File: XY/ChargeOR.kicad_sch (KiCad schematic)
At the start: 8 parts, among them U13 LTC4376CDHD_PBF, U9 SI3865DDV-T1-GE3

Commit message: MPPT fixes
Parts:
- removed C48: 10uF, Capacitor_SMD:C_1206_3216Metric, symbol Device:C_Small
- removed C49: 1nF, Capacitor_SMD:C_0603_1608Metric, symbol Device:C_Small
- removed C50: 1uF, Capacitor_SMD:C_1206_3216Metric, symbol Device:C_Small
- removed D7: LSM115, SolarPanels:DO-214BA_MCH, symbol Device:D_Schottky_Small
- removed R92: 100K, Resistor_SMD:R_0603_1608Metric, symbol Device:R_Small
- removed R93: 10K, Resistor_SMD:R_0603_1608Metric, symbol Device:R_Small
- removed U13: LTC4376CDHD_PBF, Package_DFN_QFN:DFN-16-1EP_4x5mm_P0.5mm_EP2.44x4.34mm, symbol SolarPanels:LTC4376CDHD_PBF
- removed U9: SI3865DDV-T1-GE3, Package_TO_SOT_SMD:SOT-23-6, symbol SolarPanels:SI3865DDV-T1-GE3
- added C42: 0.1uF, Capacitor_SMD:C_0603_1608Metric, symbol Device:C_Small
- added D8: PMEG4005EH, Diode_SMD:D_SOD-123F, symbol Diode:PMEG4005EH
- added U7: LTC4412xS6, Package_TO_SOT_SMD:TSOT-23-6, symbol Power_Management:LTC4412xS6
- added U8: SIRA99DP-T1-GE3, SolarPanels:MOSFET_7DP-T1-GE3_VIS, symbol Argus-Misc:SIRA99DP-T1-GE3
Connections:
- net GND: now also C42.2, U7.2 (GND), U7.3 (CTL)
- net IN: now also C42.1, D8.2 (A), U7.1 (VIN), U8.5 (D), U8.6 (D), U8.7 (D), U8.8 (D)
- net OUT: now also D8.1 (K), U7.6 (SENSE), U8.1 (S), U8.2 (S), U8.3 (S)
- new net: U7.5 (GATE), U8.4 (G)

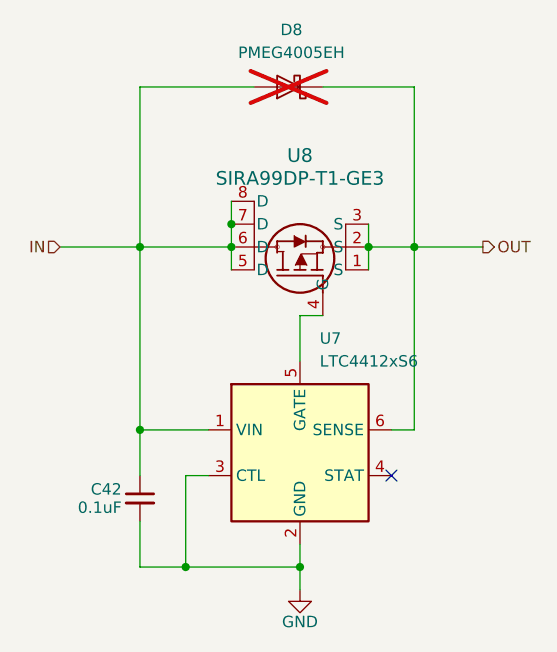
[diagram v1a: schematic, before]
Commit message: Added address breakouts
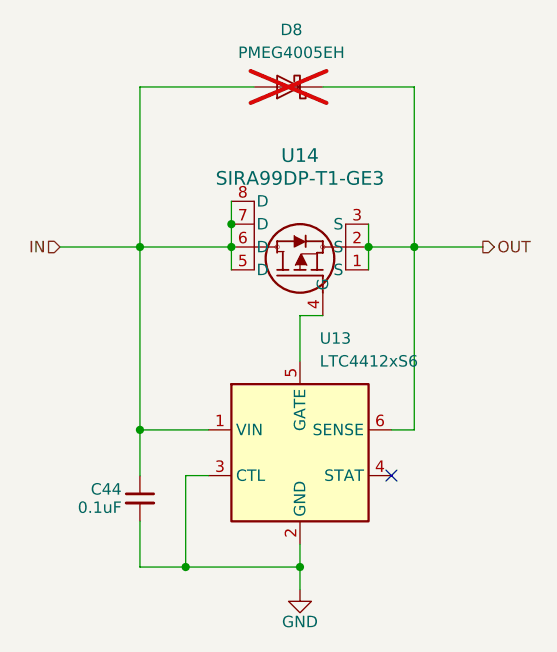
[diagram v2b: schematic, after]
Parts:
- renumbered C42 to C44, U7 to U13, U8 to U14
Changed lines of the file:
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@@
 		(on_board yes)
 		(dnp no)
-		(property "Reference" "C42"
+		(property "Reference" "C44"
 			(at 121.158 104.394 0)
 			(effects
@@
 		(dnp no)
 		(fields_autoplaced yes)
-		(property "Reference" "U7"
+		(property "Reference" "U13"
 			(at 143.1641 87.63 0)
 			(effects
@@
 		(on_board yes)
 		(dnp no)
-		(property "Reference" "#PWR018"
+		(property "Reference" "#PWR021"
 			(at 140.97 121.92 0)
 			(effects
@@
 		(dnp no)
 		(fields_autoplaced yes)
-		(property "Reference" "U8"
+		(property "Reference" "U14"
 			(at 140.97 67.31 90)
 			(effects
